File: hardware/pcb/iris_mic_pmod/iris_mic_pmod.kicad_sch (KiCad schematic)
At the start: 5 parts, among them J1 Conn_02x06_Odd_Even, U1 SPH0645LM4H

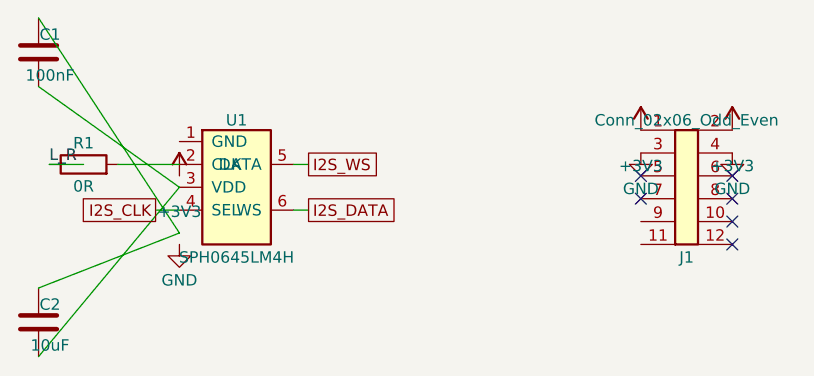
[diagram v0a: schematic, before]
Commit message: feat(hardware/pcb): route pmod board, export gerbers, add DRC reports
- Updated schematic: bidir global labels for I2S_DATA/CLK/WS, added
  second pmod connector net stubs, replaced L_R net label with GND power
  symbol on mic L/R select pin
- PCB: updated copper pour and track layout post-route
- Exported full gerber set (F/B Cu, F/B Mask, F/B Silk, Edge, drill)
- Added DRC reports — 15 violations (shorting + clearance) still open

Co-Authored-By: Claude Sonnet 4.6 <noreply@anthropic.com>
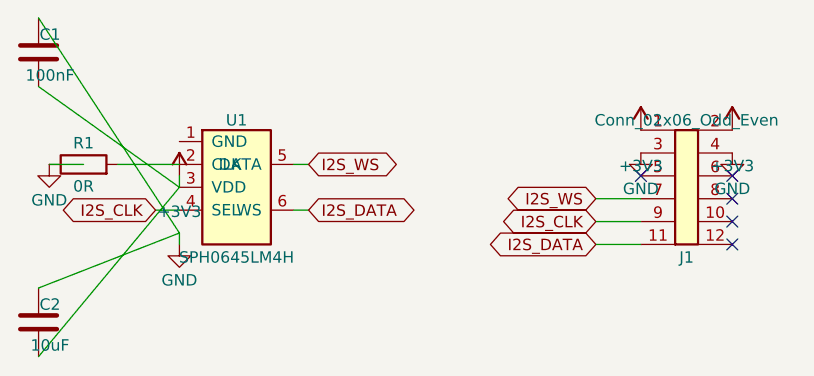
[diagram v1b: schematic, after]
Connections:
- net L_R is gone; now on net GND: R1.1
- net +3V3: now also C1.2, C2.2, U1.3 (VDD)
- net GND: now also C1.1, C2.1
- net I2S_CLK: now also J1.9 (Pin_9)
- net I2S_DATA: now also J1.11 (Pin_11)
- net I2S_WS: now also J1.7 (Pin_7)
- no-connect marks 6 -> 5
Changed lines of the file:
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@@
   (wire (pts (xy 109.19 87.46) (xy 113 87.46)) (stroke (width 0) (type default)))
   (wire (pts (xy 116.81 87.46) (xy 123.65 87.46)) (stroke (width 0) (type default)))
-  (global_label "I2S_DATA" (shape bidir) (at 138 92.54 0) (fields_autoplaced) (effects (font (size 1.27 1.27) (thickness 0.15)) (justify left)))
-  (global_label "I2S_CLK" (shape bidir) (at 121 92.54 180) (fields_autoplaced) (effects (font (size 1.27 1.27) (thickness 0.15)) (justify right)))
-  (global_label "I2S_WS" (shape bidir) (at 138 87.46 0) (fields_autoplaced) (effects (font (size 1.27 1.27) (thickness 0.15)) (justify left)))
-  (label "L_R" (at 109.19 87.46 0) (fields_autoplaced) (effects (font (size 1.27 1.27) (thickness 0.15)) (justify left bottom)))
+  (wire (pts (xy 123.65 88.73) (xy 123.65 90.00)) (stroke (width 0) (type default)))
+  (wire (pts (xy 123.65 95.08) (xy 123.65 96.35)) (stroke (width 0) (type default)))
+  (wire (pts (xy 169.92 96.35) (xy 174.92 96.35)) (stroke (width 0) (type default)))
+  (wire (pts (xy 169.92 93.81) (xy 174.92 93.81)) (stroke (width 0) (type default)))
+  (wire (pts (xy 169.92 91.27) (xy 174.92 91.27)) (stroke (width 0) (type default)))
+  (global_label "I2S_DATA" (shape bidirectional) (at 138 92.54 0) (fields_autoplaced) (effects (font (size 1.27 1.27) (thickness 0.15)) (justify left)))
+  (global_label "I2S_CLK" (shape bidirectional) (at 121 92.54 180) (fields_autoplaced) (effects (font (size 1.27 1.27) (thickness 0.15)) (justify right)))
+  (global_label "I2S_WS" (shape bidirectional) (at 138 87.46 0) (fields_autoplaced) (effects (font (size 1.27 1.27) (thickness 0.15)) (justify left)))
+  (global_label "I2S_DATA" (shape bidirectional) (at 169.92 96.35 180) (fields_autoplaced) (effects (font (size 1.27 1.27) (thickness 0.15)) (justify right)))
+  (global_label "I2S_CLK" (shape bidirectional) (at 169.92 93.81 180) (fields_autoplaced) (effects (font (size 1.27 1.27) (thickness 0.15)) (justify right)))
+  (global_label "I2S_WS" (shape bidirectional) (at 169.92 91.27 180) (fields_autoplaced) (effects (font (size 1.27 1.27) (thickness 0.15)) (justify right)))
   (no_connect (at 185.08 96.35))
   (no_connect (at 185.08 93.81))
   (no_connect (at 185.08 91.27))
   (no_connect (at 185.08 88.73))
-  (no_connect (at 174.92 91.27))
   (no_connect (at 174.92 88.73))
   (symbol (lib_id "Microphone:SPH0645LM4H") (at 130 90 0) (unit 1) (in_bom yes) (on_board yes) (dnp no) (fields_autoplaced yes)
@@
         )
       )
+    )
+  )
+  (symbol (lib_id "power:GND") (at 109.19 87.46 0) (unit 1) (in_bom yes) (on_board yes) (dnp no)
+    (property "Reference" "#PWR07" (at 109.19 93.729 0) (hide yes)
+      (effects (font (size 1.27 1.27))))
+    (property "Value" "GND" (at 109.19 91.44 0)
+      (effects (font (size 1.27 1.27))))
+    (property "Footprint" "" (at 109.19 87.46 0)
+      (effects (font (size 1.27 1.27)) (hide yes)))
+    (property "Datasheet" "" (at 109.19 87.46 0)
+      (effects (font (size 1.27 1.27)) (hide yes)))
+    (pin "1")
+    (instances
+      (project "iris_mic_pmod"
+        (path "/a1000001-0000-0000-0000-000000000000"
+          (reference "#PWR07") (unit 1)
+        )
+      )
